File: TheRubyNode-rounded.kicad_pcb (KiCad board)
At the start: 2 copper layers, 141 x 79.5 mm, 66 parts, among them J1 USB4085-GF-A_REVB, J2 Conn_02x01, J3 Conn_02x01, J4 Conn_01x02, J5 91930-21111LF, J6 Conn_01x04, J7 Conn_01x03, J8 Conn_02x01, Q1 Si2307, SW1 SW_SPST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

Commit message: Finalise rev 1.0 of PCB
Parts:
- J6: footprint Connector_JST:JST_SH_SM04B-SRSS-TB_1x04-1MP_P1.00mm_Horizontal -> Connector_JST:JST_SH_BM04B-SRSS-TB_1x04-1MP_P1.00mm_Vertical
- moved J6 0.20 mm to (133.6, 100.8)
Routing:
- net I2C_SDA: track 93.3 -> 96.7 mm
- net I2C_SCL: track 90.4 -> 93.8 mm
- net +3V3: track 173.5 -> 176.6 mm
- net GND: vias 10 -> 11
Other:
- board text added: "+5V IN"
- board text added: "+5V OUT"
- board text added: "REV v1.0"
- board text added: "USR BTN"

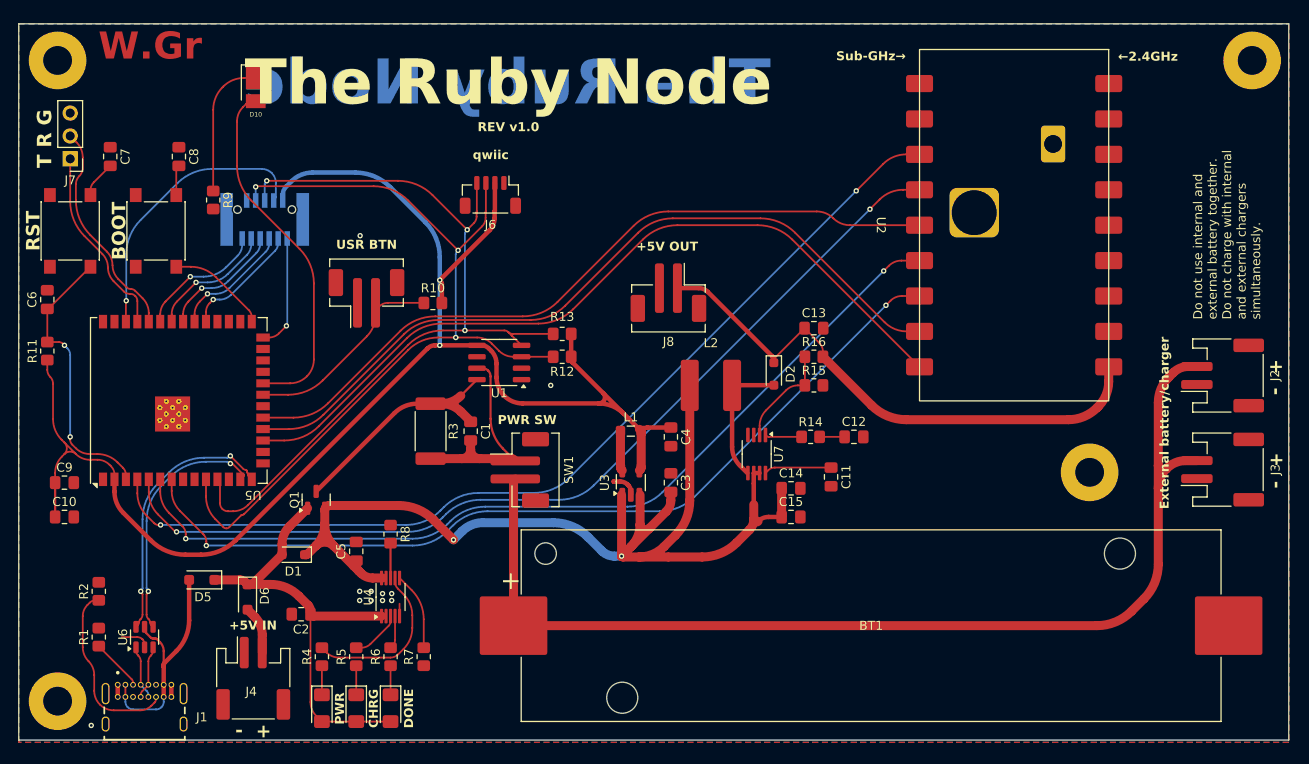
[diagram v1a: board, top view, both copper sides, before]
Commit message: Break out additional IOs
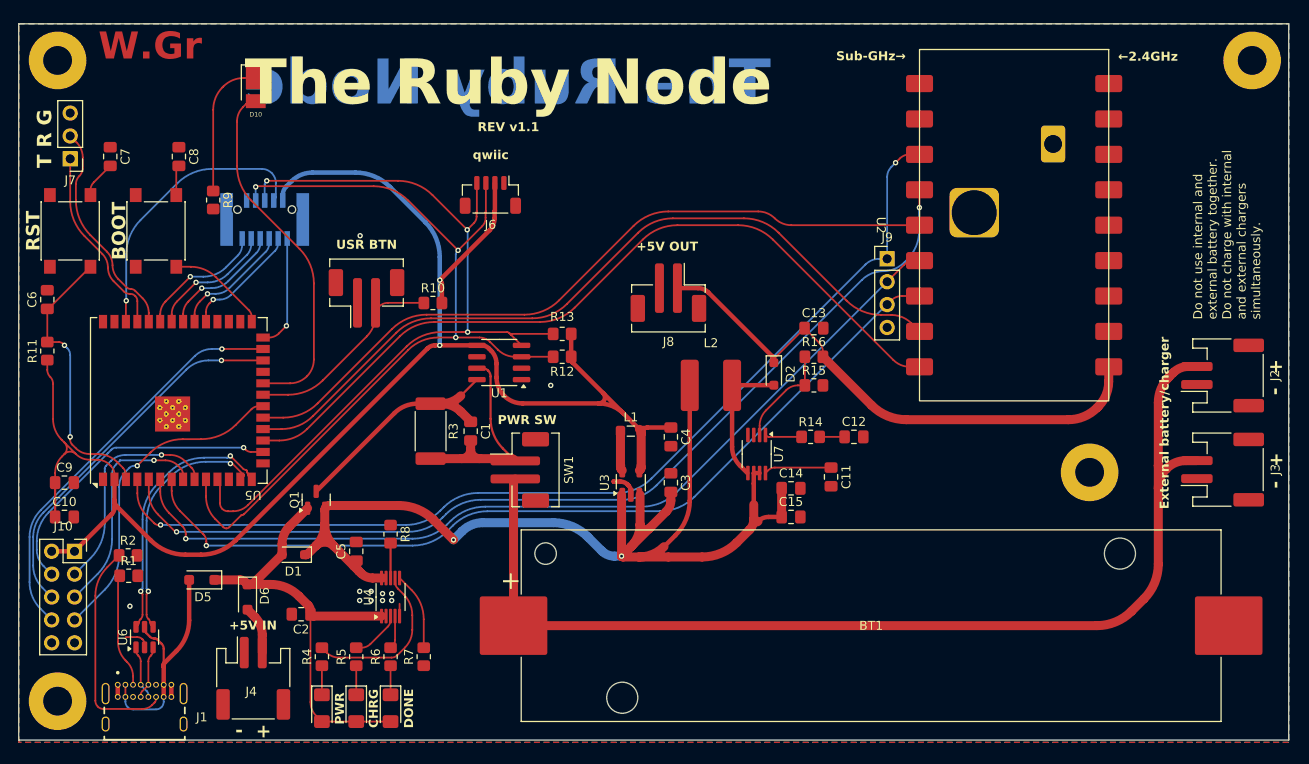
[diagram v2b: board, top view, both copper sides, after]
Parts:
- added J10: Conn_02x05_Odd_Even, Connector_PinSocket_2.54mm:PinSocket_2x05_P2.54mm_Vertical, F.Cu at (87.5, 140.3)
- added J9: Conn_01x04, Connector_PinHeader_2.54mm:PinHeader_1x04_P2.54mm_Vertical, F.Cu at (177.7, 107.9)
- moved R1 7.57 mm to (93.5, 143.1), turned to 0 degrees
- moved R2 5.15 mm to (93.4, 140.8), turned to 0 degrees
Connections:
- U5 pad 16: unconnected-(U5-IO46-Pad16) -> Net-(J10-Pin_4)
- U5 pad 20: unconnected-(U5-IO12-Pad20) -> Net-(J10-Pin_7)
- U5 pad 24: unconnected-(U5-IO47-Pad24) -> Net-(J10-Pin_6)
- U5 pad 25: unconnected-(U5-IO48-Pad25) -> Net-(J10-Pin_8)
- U5 pad 8: unconnected-(U5-IO15-Pad8) -> Net-(J10-Pin_5)
- U5 pad 9: unconnected-(U5-IO16-Pad9) -> Net-(J10-Pin_3)
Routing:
- net Net-(J10-Pin_8): track 0.00 -> 45.3 mm, vias 0 -> 1
- net Net-(J10-Pin_6): track 0.00 -> 41.6 mm, vias 0 -> 1
- net Net-(J10-Pin_7): track 0.00 -> 36.1 mm, vias 0 -> 1
- net Net-(J10-Pin_4): track 0.00 -> 34.6 mm, vias 0 -> 1
- net Net-(J10-Pin_5): track 0.00 -> 25.2 mm, vias 0 -> 1
- net Net-(J10-Pin_3): track 0.00 -> 24.9 mm, vias 0 -> 1
- net +3V3: track 176.6 -> 187.1 mm
- net Net-(J1-CC1): track 5.47 -> 12.6 mm
- net SPI_SCK: track 106.6 -> 112.2 mm
- net Net-(J1-CC2): track 20.3 -> 25.0 mm
- net LR_CS: track 104.4 -> 107.7 mm
- net SPI_MISO: track 98.5 -> 98.4 mm, vias 2 -> 1
- net SPI_MOSI: track 100.6 -> 100.7 mm, vias 2 -> 1
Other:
- board text added: "REV v1.1"
- board text removed: "REV v1.0"

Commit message: Add pin labels
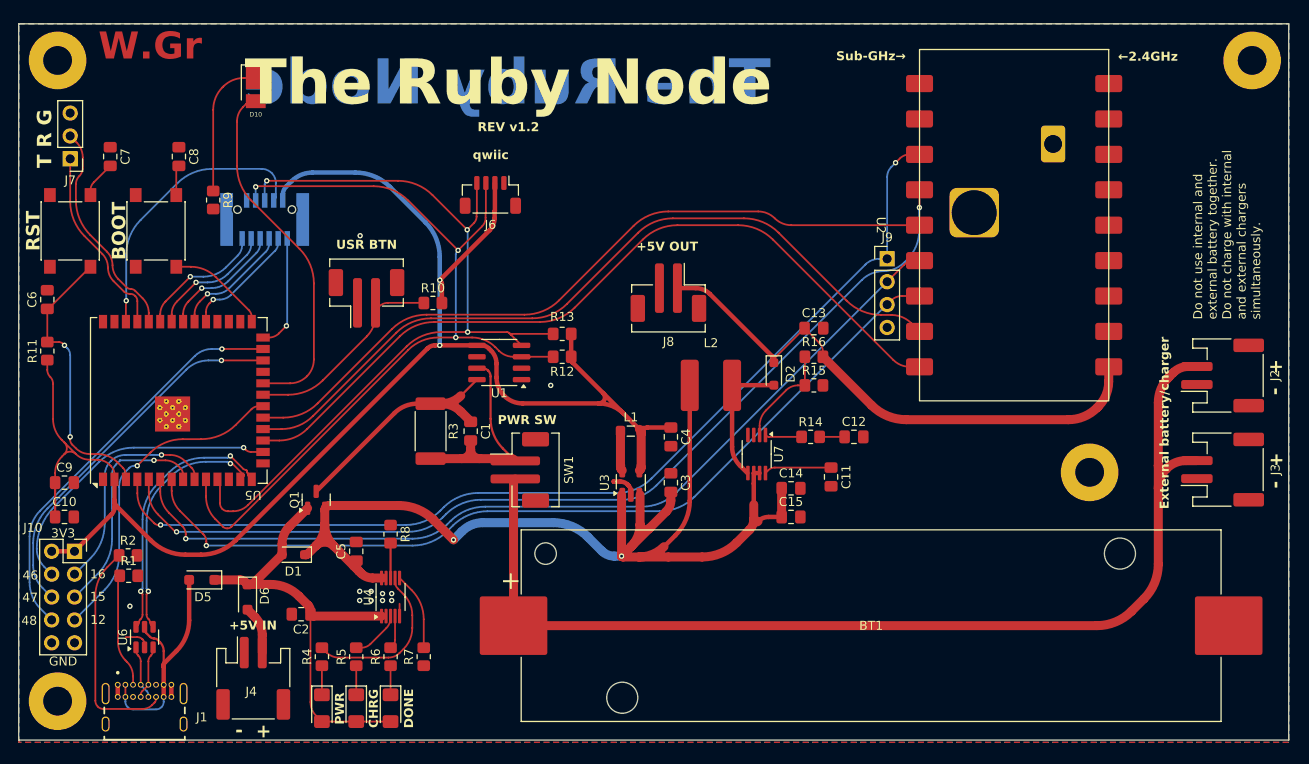
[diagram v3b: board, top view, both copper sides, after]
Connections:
- net Net-(J10-Pin_3) renamed /IO16
- net Net-(J10-Pin_4) renamed /IO46
- net Net-(J10-Pin_5) renamed /IO15
- net Net-(J10-Pin_6) renamed /IO47
- net Net-(J10-Pin_7) renamed /IO12
- net Net-(J10-Pin_8) renamed /IO48
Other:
- board text added: "12"
- board text added: "15"
- board text added: "16"
- board text added: "3V3"
- board text added: "46"
- board text added: "47"
- board text added: "48"
- board text added: "GND"
- board text added: "REV v1.2"
- board text removed: "REV v1.1"
